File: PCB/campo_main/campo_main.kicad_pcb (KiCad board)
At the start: 2 copper layers, 65 x 30 mm, 12 parts, among them J1 MOTOR 1, J2 MOTOR 2, J3 GPIO, J4 MOTOR PWR, J5 I2C, J6 Raspberry_Pi_4

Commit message: Update schematic
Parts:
- removed J6: Raspberry_Pi_4, Connector_PinSocket_2.54mm:PinSocket_2x20_P2.54mm_Vertical
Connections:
- A1 pad 25: /MISO -> /GPIO9/SPI0.MISO
- A1 pad 26: /MOSI -> /GPIO10/SPI0.MOSI
- A1 pad 27: /CSn -> /GPIO8/SPI0.CE0
- A1 pad 29: /SCK -> /GPIO11/SPI0.SCLK
- J3 pad 1: +3V3 -> +3.3V
- J3 pad 17: +3V3 -> +3.3V

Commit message: PCB update
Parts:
- removed MH1: MountingHole_2.7mm_M2.5, MountingHole:MountingHole_2.7mm_M2.5
- added J6: UART, Connector_PinSocket_2.54mm:PinSocket_1x04_P2.54mm_Vertical, F.Cu at (159.6, 77.3)
- added J7: I2C, Connector_PinSocket_2.54mm:PinSocket_1x04_P2.54mm_Vertical, F.Cu at (159.7, 58.5)
- moved J1 111.6 mm to (111.9, 97.2), turned to 90 degrees
- moved J2 108.1 mm to (140.9, 97.2), turned to -90 degrees
- moved J5 75.7 mm to (117.5, 78.8), turned to -90 degrees
- moved J4 75.4 mm to (104.0, 86.7), turned to 90 degrees
- moved U1 40.8 mm to (126.7, 86.5), turned to 90 degrees
- moved MH2 26.0 mm to (161.5, 47.5)
- moved J3 26.0 mm to (108.4, 48.8)
- moved A1 23.6 mm to (125.8, 64.8)
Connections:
- A1 pad 1: /SDA -> /GPIO14/TXD0
- A1 pad 10: Net-(A1-GPIO7) -> /IN3
- A1 pad 11: Net-(A1-GPIO8) -> /IN2
- A1 pad 12: unconnected-(A1-GPIO9-Pad12) -> /IN1
- A1 pad 14: unconnected-(A1-GPIO10-Pad14) -> /EEP
- A1 pad 15: /EN1A -> /ULT
- A1 pad 16: unconnected-(A1-GPIO12-Pad16) -> /G6
- A1 pad 17: /EN1B -> /EN2A
- A1 pad 19: unconnected-(A1-GPIO14-Pad19) -> /EN2B
- A1 pad 2: /SCL -> /GPIO15/RXD0
- A1 pad 20: /EN2B -> /G15
- A1 pad 21: unconnected-(A1-GPIO16-Pad21)_1 -> /GPIO10/SPI0.MOSI
- A1 pad 22: /EN2A -> /GPIO8/SPI0.CE0
- A1 pad 24: unconnected-(A1-GPIO18-Pad24) -> /GPIO11/SPI0.SCLK
- A1 pad 26: /GPIO10/SPI0.MOSI -> unconnected-(A1-GPIO20-Pad26)
- A1 pad 27: /GPIO8/SPI0.CE0 -> unconnected-(A1-GPIO21-Pad27)
- A1 pad 29: /GPIO11/SPI0.SCLK -> unconnected-(A1-GPIO22-Pad29)
- A1 pad 33: unconnected-(A1-AGND-Pad33) -> GND
- A1 pad 4: unconnected-(A1-GPIO2-Pad4) -> /EN1A
- A1 pad 5: Net-(A1-GPIO3) -> /EN1B
- A1 pad 6: Net-(A1-GPIO4) -> /SDA
- A1 pad 7: Net-(A1-GPIO5) -> /SCL
- A1 pad 9: Net-(A1-GPIO6) -> /IN4
- J1 pad 1: /M1 -> GND
- J1 pad 2: /M2 -> /EN1B
- J1 pad 3: +3.3V -> /EN1A
- J1 pad 4: /EN1A -> +3.3V
- J1 pad 5: /EN1B -> /M2
- J1 pad 6: GND -> /M1
- J2 pad 1: /M3 -> GND
- J2 pad 2: /M4 -> /EN2B
- J2 pad 3: +3.3V -> /EN2A
- J2 pad 4: /EN2A -> +3.3V
- J2 pad 5: /EN2B -> /M4
- J2 pad 6: GND -> /M3
- J3 pad 1: +3.3V -> unconnected-(J3-Pin_1-Pad1)
- J3 pad 17: +3.3V -> unconnected-(J3-Pin_17-Pad17)
- J5 pad 2: /SDA -> +3.3V
- J5 pad 4: +3.3V -> /SDA
- U1 pad 1: Net-(A1-GPIO3) -> /EEP
- U1 pad 11: Net-(A1-GPIO6) -> /IN3
- U1 pad 12: Net-(A1-GPIO7) -> /IN4
- U1 pad 6: Net-(A1-GPIO8) -> /ULT
- U1 pad 7: Net-(A1-GPIO4) -> /IN1
- U1 pad 8: Net-(A1-GPIO5) -> /IN2
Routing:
- net +3.3V: track 0.00 -> 145.9 mm
- net /GPIO14/TXD0: track 0.00 -> 90.1 mm, vias 0 -> 2
- net /GPIO15/RXD0: track 0.00 -> 85.8 mm
- net /GPIO2/SDA1: track 0.00 -> 61.0 mm
- net /GPIO3/SCL1: track 0.00 -> 56.0 mm, vias 0 -> 1
- net +5V: track 0.00 -> 29.4 mm
- net /EN1B: track 0.00 -> 28.6 mm, vias 0 -> 1
- net /EN2B: track 0.00 -> 27.3 mm
- net Net-(J4-Pin_1): track 0.00 -> 27.2 mm
- net /EN1A: track 0.00 -> 26.8 mm
- net /EEP: track 0.00 -> 25.6 mm
- net /EN2A: track 0.00 -> 25.4 mm
- net /GPIO10/SPI0.MOSI: track 0.00 -> 24.7 mm
- net /ULT: track 0.00 -> 22.2 mm
- net /GPIO8/SPI0.CE0: track 0.00 -> 15.7 mm
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- added copper zone on B.Cu, net GND
- added copper zone on F.Cu, net GND
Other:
- board size 65 x 30 mm -> 65 x 56 mm
- board text added: "2"
- board text added: "3.3V"
- board text added: "CAMERA (OPTIONAL)"
- board text added: "Campo Lampone 2025"
- board text added: "ENA"
- board text added: "ENB"
- board text added: "GND"
- board text added: "I C"
- board text added: "M1"
- board text added: "M2"
- board text added: "M3"
- board text added: "M4"
- board text added: "MOTOR VIN (2.7-10.8V)"
- board text added: "Made with by Plajta"
- board text added: "RJ45"
- board text added: "RPI PICO"
- board text added: "RX"
- board text added: "SCL"
- board text added: "SDA"
- board text added: "SSD1306"
- board text added: "TX"
- board text added: "UART"
- board text added: "USB"
- board text removed: "Extend PCB edge 0.5mm if using SMT header"
- board text removed: "PoE"

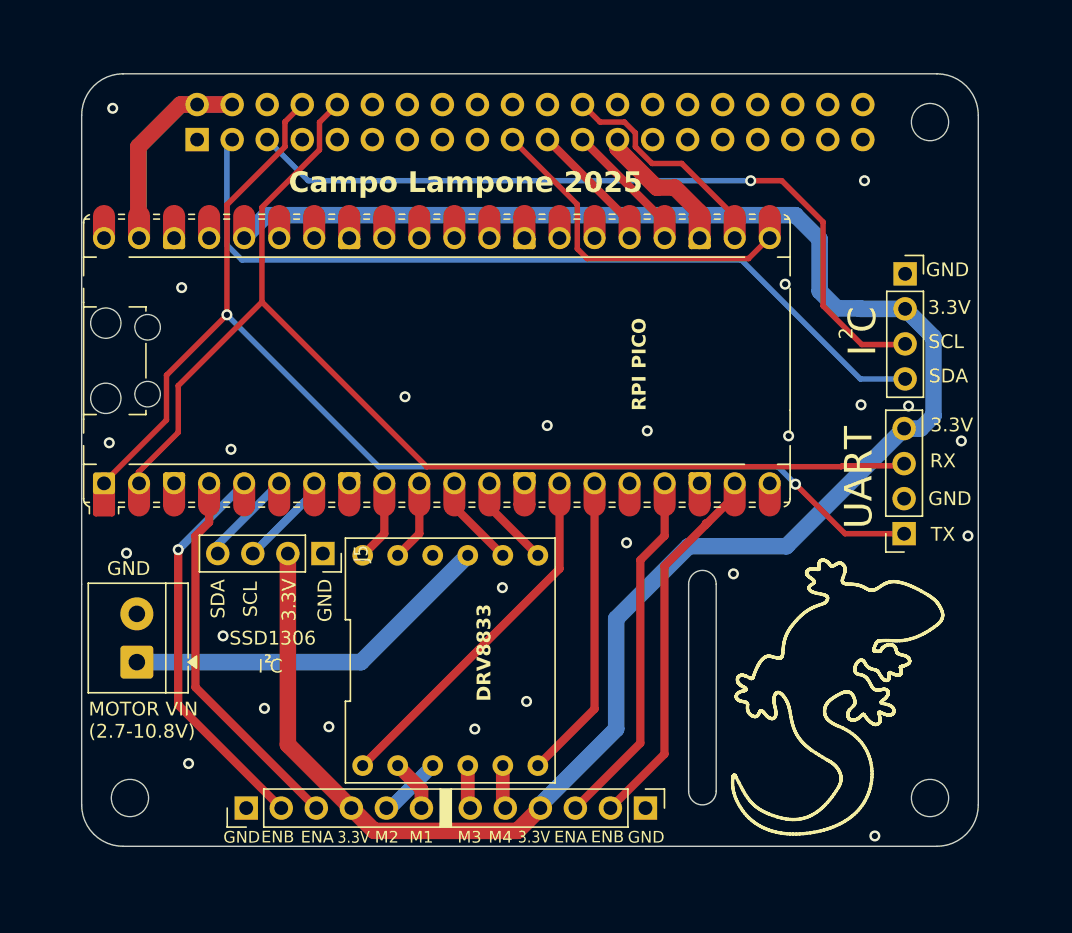
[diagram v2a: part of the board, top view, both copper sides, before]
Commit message: Upgrade silkscreen
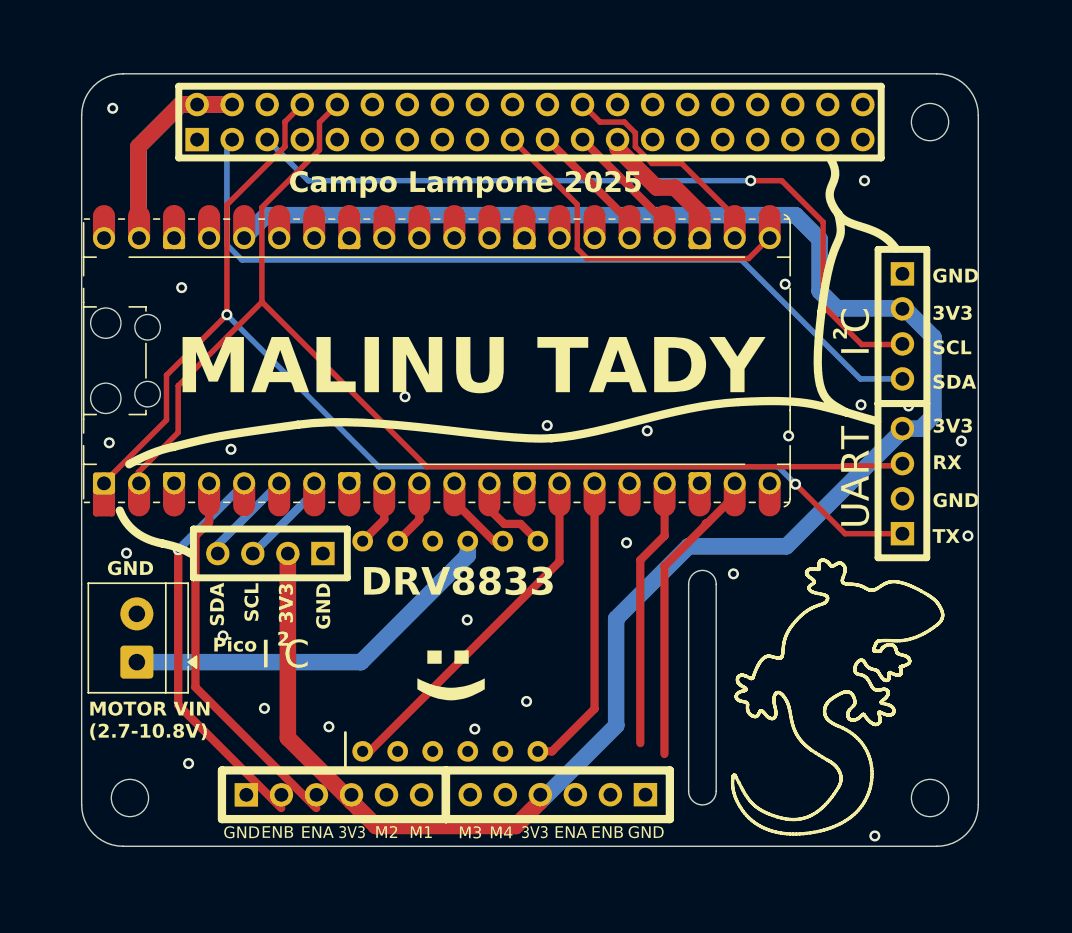
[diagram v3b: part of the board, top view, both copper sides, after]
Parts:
- J5, J6, J7: footprint Connector_PinSocket_2.54mm:PinSocket_1x04_P2.54mm_Vertical -> Connector_PinHeader_2.54mm:PinHeader_1x04_P2.54mm_Vertical
- moved U1 1.03 mm to (126.7, 85.5)
- moved J2 0.97 mm to (140.9, 96.3)
- moved J1 0.96 mm to (111.9, 96.3)
- moved J7 0.19 mm to (159.5, 58.5)
- moved J6 0.12 mm to (159.5, 77.3)
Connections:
- net Net-(J4-Pin_1) renamed /MVIN
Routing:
- net /EN2A: track 25.4 -> 18.8 mm
- net /EN2B: track 27.3 -> 21.8 mm
- net /M2: track 4.64 -> 0.00 mm
- net /M1: track 3.79 -> 0.00 mm
- net /M3: track 3.35 -> 0.00 mm
- net /M4: track 3.35 -> 0.00 mm
- net /IN3: track 5.87 -> 4.04 mm
- net +3.3V: track 145.9 -> 144.5 mm
- net /MVIN: track 27.2 -> 28.2 mm
- net /IN4: track 5.07 -> 4.04 mm
- net /EEP: track 25.6 -> 24.8 mm
- net /IN2: track 5.87 -> 5.22 mm
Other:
- board text added: "3V3"
- board text added: ":)"
- board text added: "MALINU TADY"
- board text added: "Pico"
- board text removed: "3.3V"
- board text removed: "RPI PICO"
- board text removed: "SSD1306"

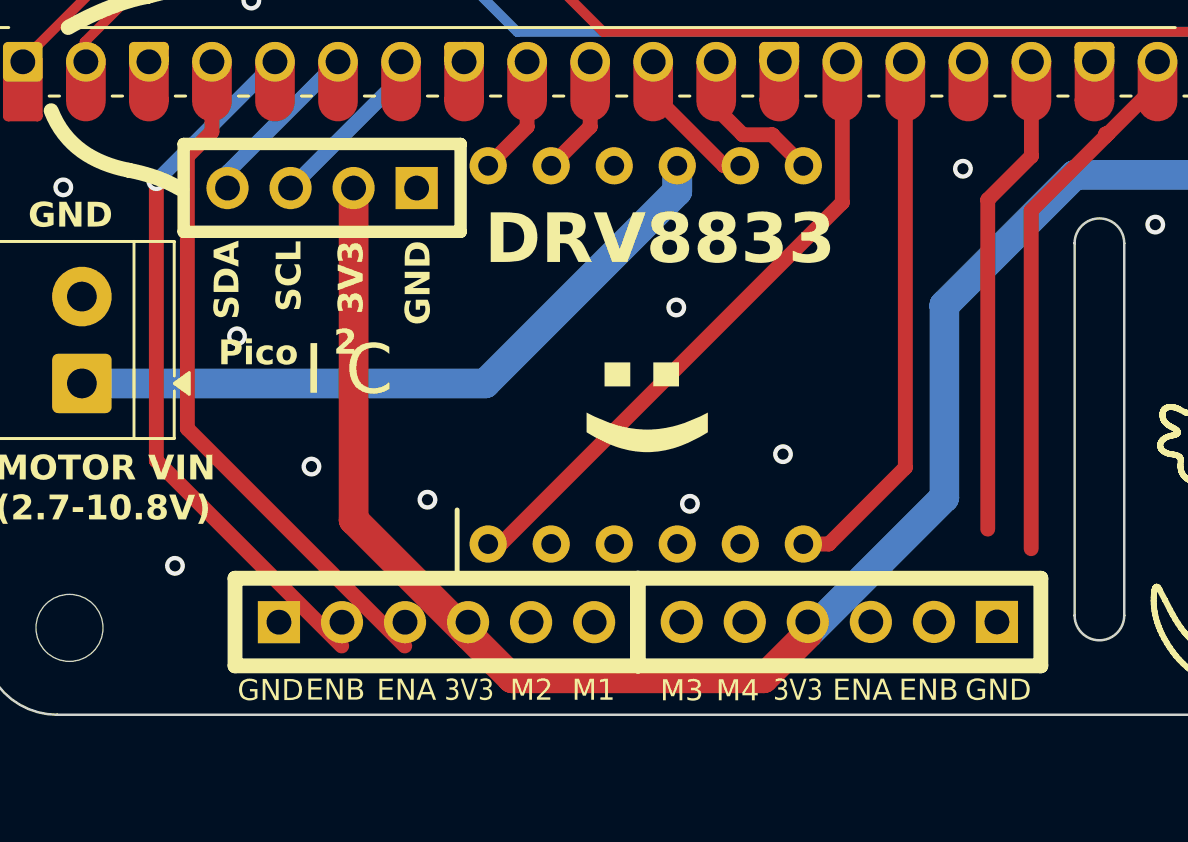
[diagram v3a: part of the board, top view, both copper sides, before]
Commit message: Fix broken traces
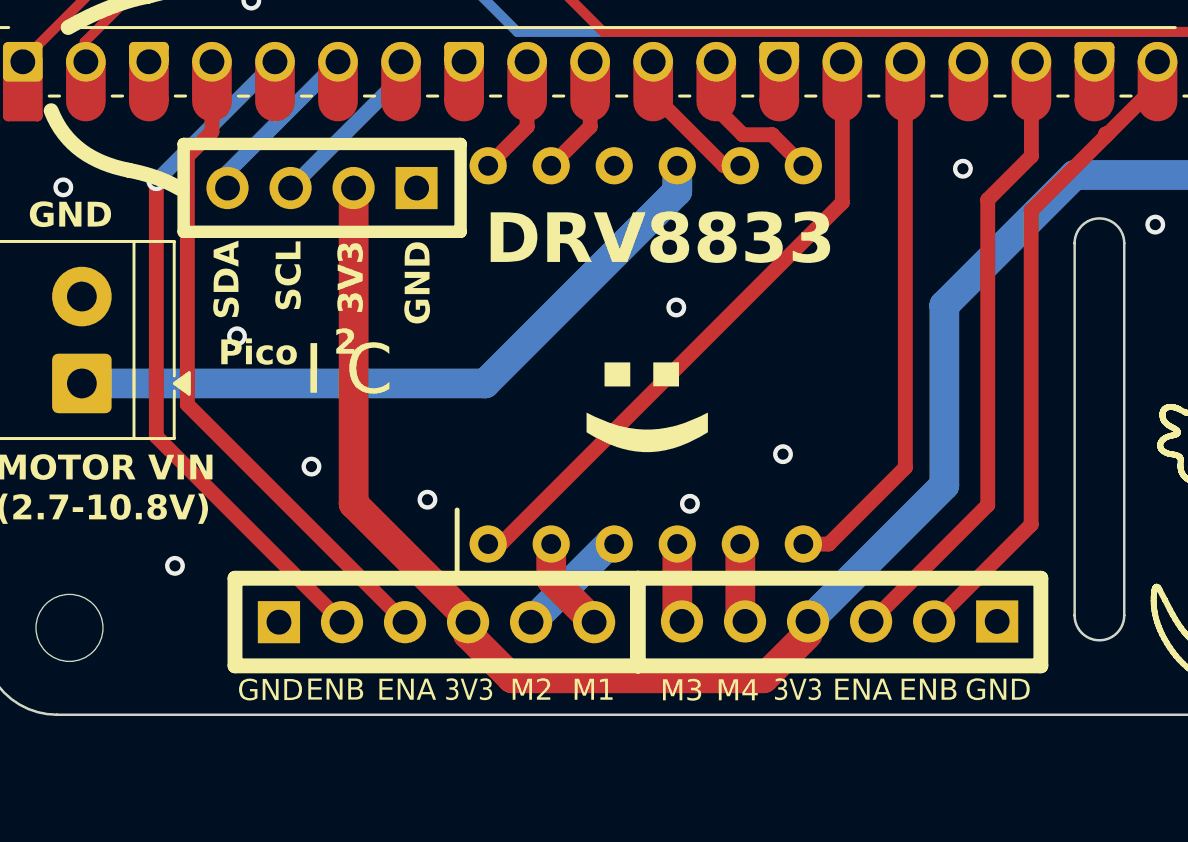
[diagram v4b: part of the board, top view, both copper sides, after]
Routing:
- net /EN2A: track 18.8 -> 24.4 mm
- net /M2: track 0.00 -> 4.65 mm
- net /EN2B: track 21.8 -> 26.3 mm
- net /M1: track 0.00 -> 3.87 mm
- net /M3: track 0.00 -> 3.22 mm
- net /M4: track 0.00 -> 3.22 mm
- net /EN1A: track 26.8 -> 25.8 mm
- net /EN1B: track 28.6 -> 27.7 mm
- net +3.3V: track 144.5 -> 144.0 mm

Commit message: Fix for PCB
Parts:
- moved J4 3.52 mm to (104.0, 83.1), turned to -90 degrees
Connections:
- A1 pad 1: /GPIO14/TXD0 -> /TX
- A1 pad 16: /G6 -> unconnected-(A1-GPIO12-Pad16)
- A1 pad 2: /GPIO15/RXD0 -> /RX
- A1 pad 20: /G15 -> unconnected-(A1-GPIO15-Pad20)
- A1 pad 26: unconnected-(A1-GPIO20-Pad26) -> /GPIO15/RXD0
- A1 pad 27: unconnected-(A1-GPIO21-Pad27) -> /GPIO14/TXD0
- J4 pad 1: /MVIN -> GND
- J4 pad 2: GND -> /MVIN
- J6 pad 1: /GPIO14/TXD0 -> /TX
- J6 pad 3: /GPIO15/RXD0 -> /RX
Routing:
- net /GPIO14/TXD0: track 90.0 -> 22.9 mm, vias 2 -> 0
- net /GPIO15/RXD0: track 85.8 -> 23.9 mm
- net /TX: track 0.00 -> 60.6 mm, vias 0 -> 1
- net /RX: track 0.00 -> 56.4 mm

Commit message: Some PCB Changes
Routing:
- net +3.3V: track 144.0 -> 141.5 mm
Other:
- board text added: "0 TX"
- board text added: "1 RX"
- board text added: "10 EEP"
- board text added: "11 ULT"
- board text added: "13 EN2A"
- board text added: "14 EN2B"
- board text added: "2 EN1A"
- board text added: "3 EN1B"
- board text added: "4 SDA"
- board text added: "5 SCL"
- board text added: "6 IN4"
- board text added: "7 IN3"
- board text added: "8 IN2"
- board text added: "9 IN1"
- board text added: "CSn 17"
- board text added: "DEBUG"
- board text added: "Docs for real"
- board text added: "Encoder 1"
- board text added: "Encoder 2"
- board text added: "FROM 40 PIN"
- board text added: "MISO 19"
- board text added: "MOSI 16"
- board text added: "Motor DRW"
- board text added: "Oled"
- board text added: "PICO PINOUT"
- board text added: "RX 22"
- board text added: "SCLK 18"
- board text added: "TX 21"
- board text added: "To 40pin"
- board text added: "Uart 0"

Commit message: PCB final
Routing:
- net GND: vias 25 -> 21
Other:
- board text added: "Pico I C"
- board text removed: ":)"
- board text removed: "Pico"
